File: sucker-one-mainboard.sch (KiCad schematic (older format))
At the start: 114 parts, among them J1 JST NC Valve, J10 JST Motor, J11 User Interface Module, J12 SWD, J2 JST NO Valve, J3 6P4C, J4 JST 3 Way Valve, J5 EXP Port, Q1 BSS138, Q2 BSS138, Q3 BSS138, Q4 DMN15H310SE-13, SW1 Power Switch, SW2 Reset, U1 LD1117S33TR, U2 TPS61087DRCR, U3 STM32F103RBTx, U4 2SMPP-03, U5 INA125UA, Y1 8MHz(16pf)

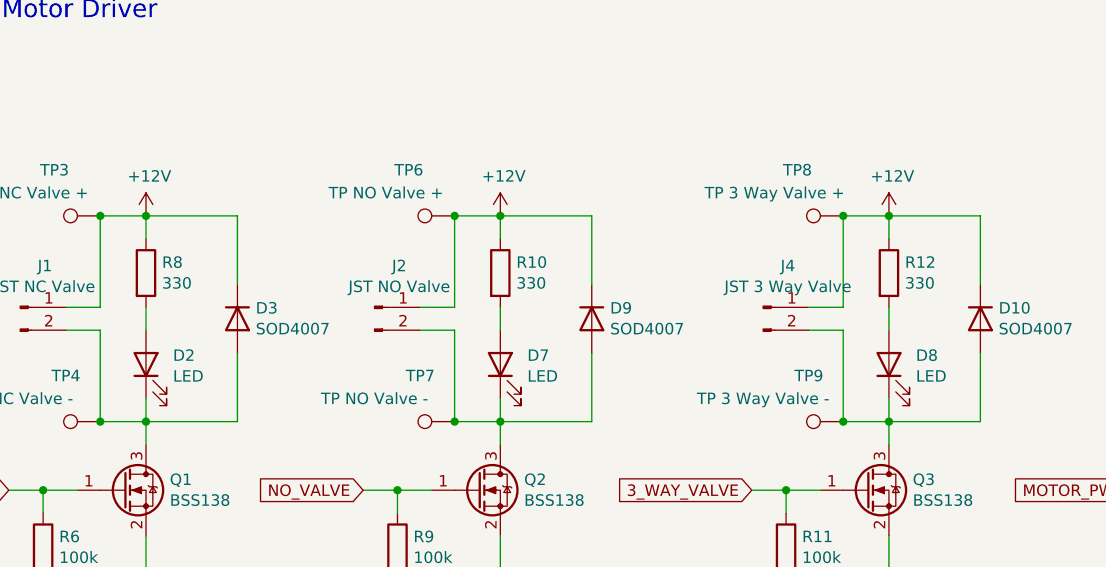
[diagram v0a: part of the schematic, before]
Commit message: Dim LEDs by increasing their resistor values
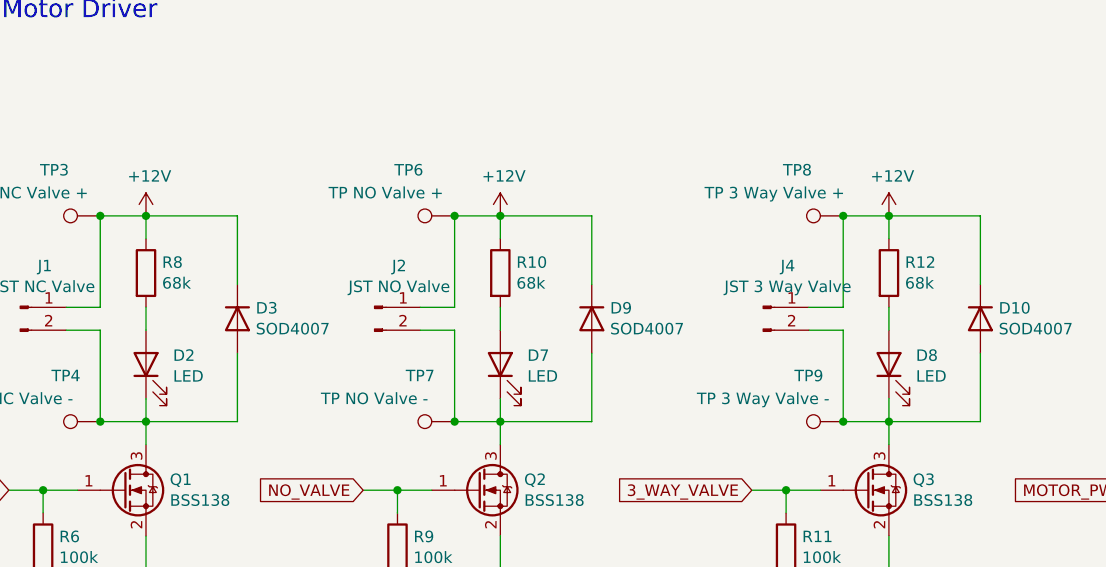
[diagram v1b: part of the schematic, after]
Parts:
- R10, R12, R8: value 330 -> 68k
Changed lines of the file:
@@
 P 4550 1750
 F 0 "R8" H 4620 1796 50  0000 L CNN
-F 1 "330" H 4620 1705 50  0000 L CNN
+F 1 "68k" H 4620 1705 50  0000 L CNN
 F 2 "Resistor_SMD:R_0603_1608Metric_Pad0.98x0.95mm_HandSolder" V 4480 1750 50  0001 C CNN
 F 3 "~" H 4550 1750 50  0001 C CNN
@@
 P 6100 1750
 F 0 "R10" H 6170 1796 50  0000 L CNN
-F 1 "330" H 6170 1705 50  0000 L CNN
+F 1 "68k" H 6170 1705 50  0000 L CNN
 F 2 "Resistor_SMD:R_0603_1608Metric_Pad0.98x0.95mm_HandSolder" V 6030 1750 50  0001 C CNN
 F 3 "~" H 6100 1750 50  0001 C CNN
@@
 P 7800 1750
 F 0 "R12" H 7870 1796 50  0000 L CNN
-F 1 "330" H 7870 1705 50  0000 L CNN
+F 1 "68k" H 7870 1705 50  0000 L CNN
 F 2 "Resistor_SMD:R_0603_1608Metric_Pad0.98x0.95mm_HandSolder" V 7730 1750 50  0001 C CNN
 F 3 "~" H 7800 1750 50  0001 C CNN

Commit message: Fix both fuse footprints (they were swapped)
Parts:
- F1: footprint Fuse:Fuse_1210_3225Metric_Pad1.42x2.65mm_HandSolder -> Fuse:Fuse_1812_4532Metric_Pad1.30x3.40mm_HandSolder
- F2: footprint Fuse:Fuse_1812_4532Metric_Pad1.30x3.40mm_HandSolder -> Fuse:Fuse_1210_3225Metric_Pad1.42x2.65mm_HandSolder
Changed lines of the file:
@@
 F 0 "F2" V 3425 8300 50  0000 C CNN
 F 1 "1210L150THWR" V 3334 8300 50  0000 C CNN
-F 2 "Fuse:Fuse_1812_4532Metric_Pad1.30x3.40mm_HandSolder" H 3250 8100 50  0001 L CNN
+F 2 "Fuse:Fuse_1210_3225Metric_Pad1.42x2.65mm_HandSolder" H 3250 8100 50  0001 L CNN
 F 3 "~" H 3200 8300 50  0001 C CNN
 F 4 "" V 3200 8300 50  0001 C CNN "Field4"
@@
 F 0 "F1" V 3150 6750 50  0000 C CNN
 F 1 "1812L075PR" V 3050 6550 50  0000 C CNN
-F 2 "Fuse:Fuse_1210_3225Metric_Pad1.42x2.65mm_HandSolder" H 3250 6350 50  0001 L CNN
+F 2 "Fuse:Fuse_1812_4532Metric_Pad1.30x3.40mm_HandSolder" H 3250 6350 50  0001 L CNN
 F 3 "~" H 3200 6550 50  0001 C CNN
 F 4 "" V 3200 6550 50  0001 C CNN "Field4"

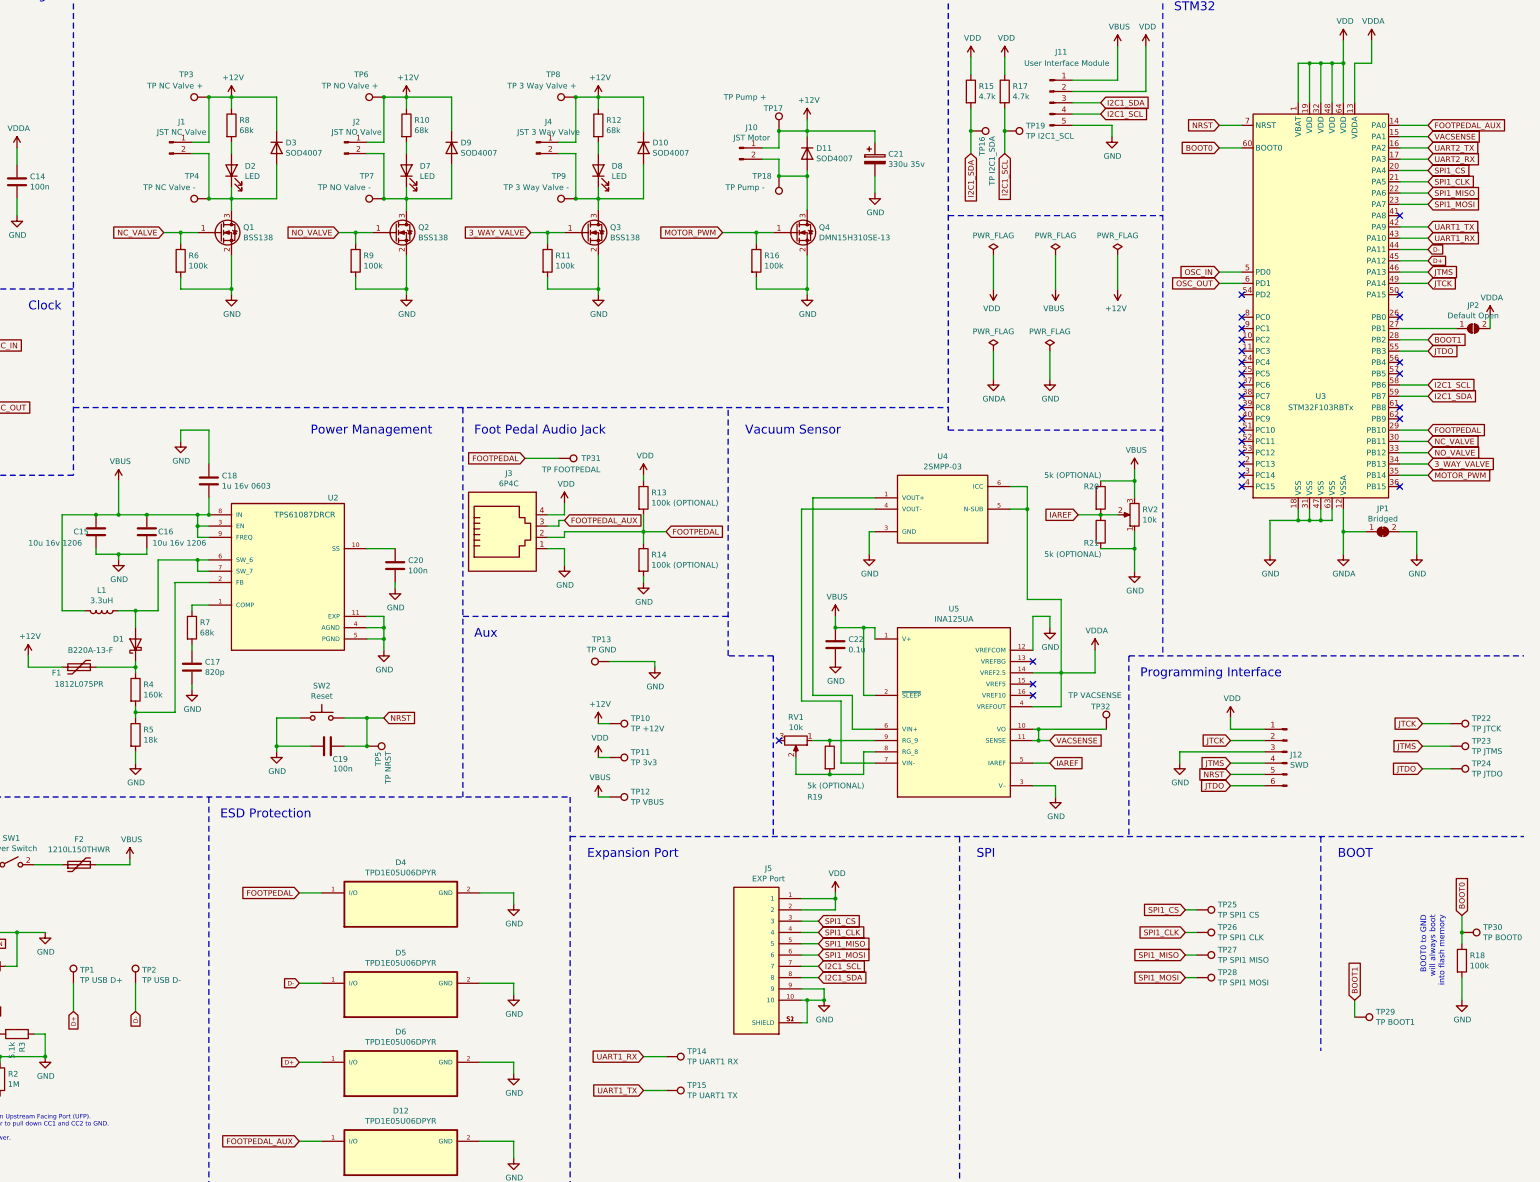
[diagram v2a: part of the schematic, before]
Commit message: Update silkscreen labels
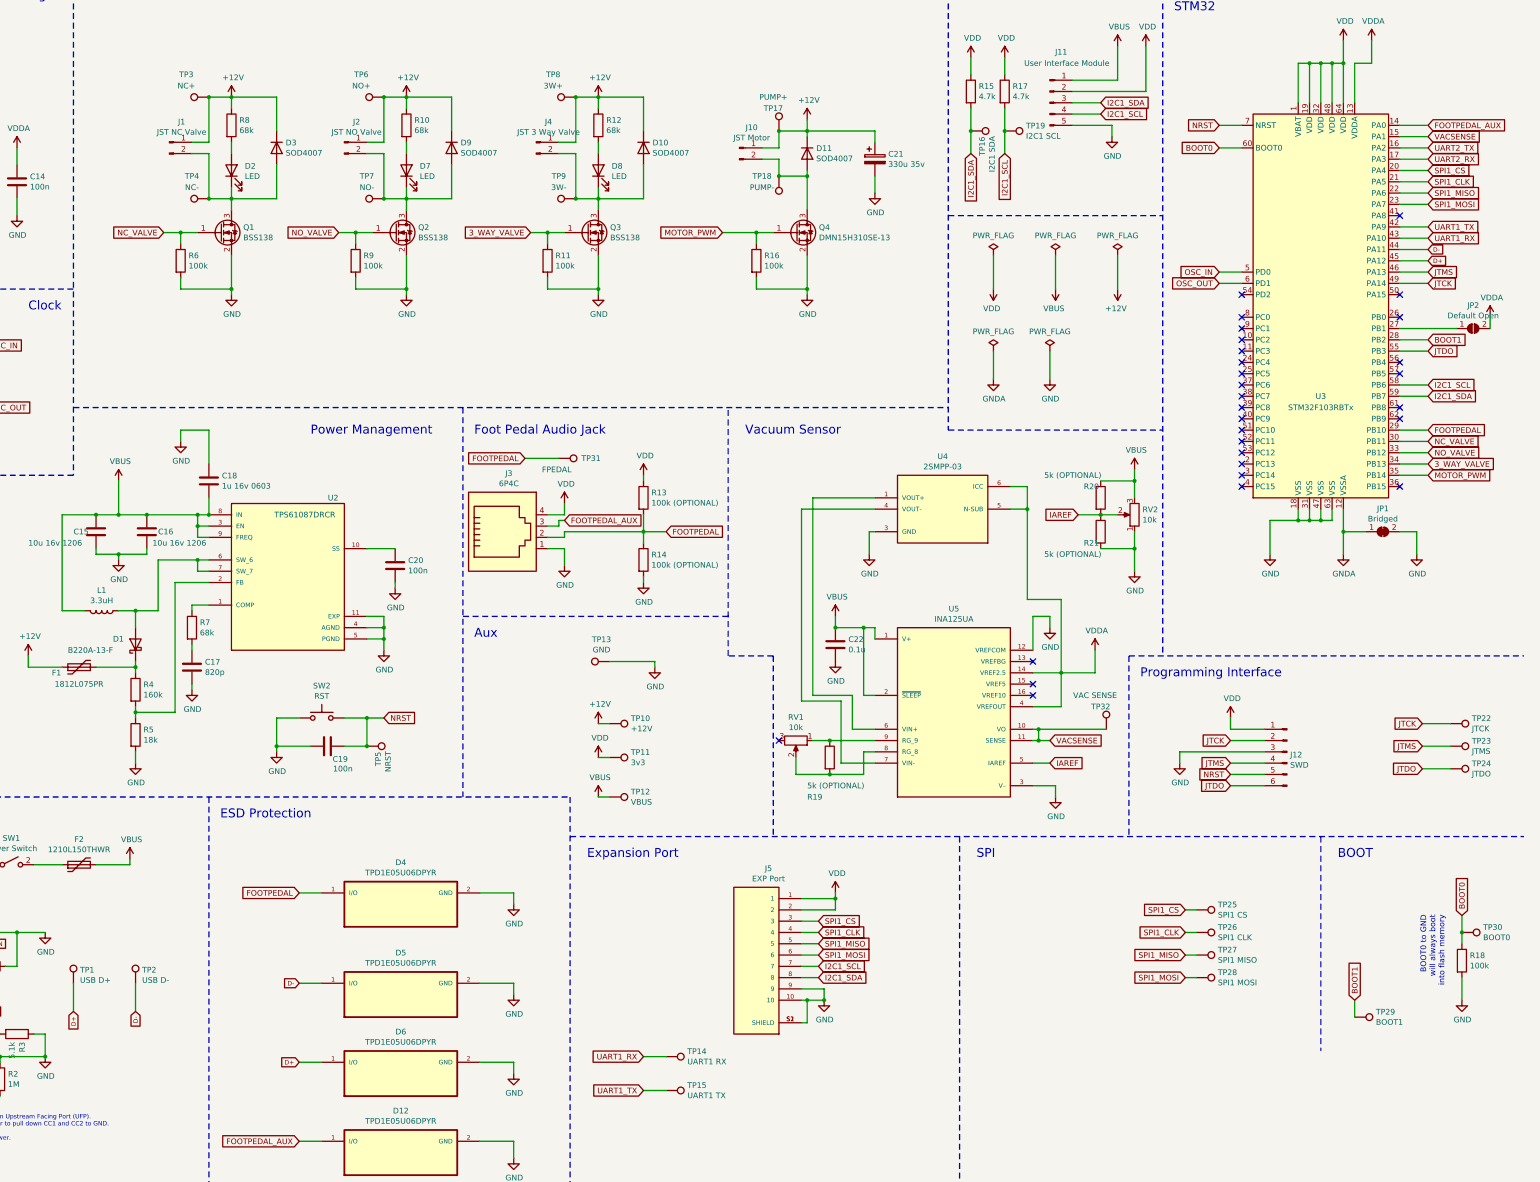
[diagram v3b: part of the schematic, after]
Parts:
- SW2: value Reset -> RST
- TP1: value TP USB D+ -> USB D+
- TP10: value TP +12V -> +12V
- TP11: value TP 3v3 -> 3v3
- TP12: value TP VBUS -> VBUS
- TP13: value TP GND -> GND
- TP14: value TP UART1 RX -> UART1 RX
- TP15: value TP UART1 TX -> UART1 TX
- TP16: value TP I2C1_SDA -> I2C1 SDA
- TP17: value TP Pump + -> PUMP+
- TP18: value TP Pump - -> PUMP-
- TP19: value TP I2C1_SCL -> I2C1 SCL
- TP2: value TP USB D- -> USB D-
- TP22: value TP JTCK -> JTCK
- TP23: value TP JTMS -> JTMS
- TP24: value TP JTDO -> JTDO
- TP25: value TP SPI1 CS -> SPI1 CS
- TP26: value TP SPI1 CLK -> SPI1 CLK
- TP27: value TP SPI1 MISO -> SPI1 MISO
- TP28: value TP SPI1 MOSI -> SPI1 MOSI
- TP29: value TP BOOT1 -> BOOT1
- TP3: value TP NC Valve + -> NC+
- TP30: value TP BOOT0 -> BOOT0
- TP31: value TP FOOTPEDAL -> FPEDAL
- TP32: value TP VACSENSE -> VAC SENSE
- TP4: value TP NC Valve - -> NC-
- TP5: value TP NRST -> NRST
- TP6: value TP NO Valve + -> NO+
- TP7: value TP NO Valve - -> NO-
- TP8: value TP 3 Way Valve + -> 3W+
- TP9: value TP 3 Way Valve - -> 3W-
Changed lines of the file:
@@
 P 5350 7000
 F 0 "SW2" H 5350 7285 50  0000 C CNN
-F 1 "Reset" H 5350 7194 50  0000 C CNN
+F 1 "RST" H 5350 7194 50  0000 C CNN
 F 2 "Button_Switch_SMD:SW_SPST_B3U-1000P" H 5350 7200 50  0001 C CNN
 F 3 "~" H 5350 7200 50  0001 C CNN
@@
 P 7900 7050
 F 0 "TP10" V 7854 7238 50  0000 L CNN
-F 1 "TP +12V" V 7945 7238 50  0000 L CNN
+F 1 "+12V" V 7945 7238 50  0000 L CNN
 F 2 "TestPoint:TestPoint_Pad_D2.0mm" H 8100 7050 50  0001 C CNN
 F 3 "~" H 8100 7050 50  0001 C CNN
@@
 P 7900 7350
 F 0 "TP11" V 7854 7538 50  0000 L CNN
-F 1 "TP 3v3" V 7945 7538 50  0000 L CNN
+F 1 "3v3" V 7945 7538 50  0000 L CNN
 F 2 "TestPoint:TestPoint_Pad_D2.0mm" H 8100 7350 50  0001 C CNN
 F 3 "~" H 8100 7350 50  0001 C CNN
@@
 P 7900 7700
 F 0 "TP12" V 7854 7888 50  0000 L CNN
-F 1 "TP VBUS" V 7945 7888 50  0000 L CNN
+F 1 "VBUS" V 7945 7888 50  0000 L CNN
 F 2 "TestPoint:TestPoint_Pad_D2.0mm" H 8100 7700 50  0001 C CNN
 F 3 "~" H 8100 7700 50  0001 C CNN
@@
 P 11400 1800
 F 0 "TP19" V 11354 1988 50  0000 L CNN
-F 1 "TP I2C1_SCL" V 11445 1988 50  0000 L CNN
+F 1 "I2C1 SCL" V 11445 1988 50  0000 L CNN
 F 2 "TestPoint:TestPoint_Pad_D2.0mm" H 11600 1800 50  0001 C CNN
 F 3 "~" H 11600 1800 50  0001 C CNN
@@
 P 11100 1800
 F 0 "TP16" H 11150 1900 50  0000 L CNN
-F 1 "TP I2C1_SDA" H 11145 1988 50  0000 L CNN
+F 1 " I2C1 SDA" H 11145 1988 50  0000 L CNN
 F 2 "TestPoint:TestPoint_Pad_D2.0mm" H 11300 1800 50  0001 C CNN
 F 3 "~" H 11300 1800 50  0001 C CNN
@@
 P 4350 1500
 F 0 "TP3" V 4550 1700 50  0000 C CNN
-F 1 "TP NC Valve +" V 4450 1800 50  0000 C CNN
+F 1 "NC+" V 4450 1700 50  0000 C CNN
 F 2 "TestPoint:TestPoint_Pad_D2.0mm" H 4550 1500 50  0001 C CNN
 F 3 "~" H 4550 1500 50  0001 C CNN
@@
 P 4350 2400
 F 0 "TP4" V 4550 2550 50  0000 C CNN
-F 1 "TP NC Valve -" V 4450 2750 50  0000 C CNN
+F 1 "NC-" V 4450 2550 50  0000 C CNN
 F 2 "TestPoint:TestPoint_Pad_D2.0mm" H 4550 2400 50  0001 C CNN
 F 3 "~" H 4550 2400 50  0001 C CNN
@@
 P 5900 2400
 F 0 "TP7" V 6100 2550 50  0000 C CNN
-F 1 "TP NO Valve -" V 6000 2750 50  0000 C CNN
+F 1 "NO-" V 6000 2550 50  0000 C CNN
 F 2 "TestPoint:TestPoint_Pad_D2.0mm" H 6100 2400 50  0001 C CNN
 F 3 "~" H 6100 2400 50  0001 C CNN
@@
 P 5900 1500
 F 0 "TP6" V 6100 1700 50  0000 C CNN
-F 1 "TP NO Valve +" V 6000 1800 50  0000 C CNN
+F 1 "NO+" V 6000 1700 50  0000 C CNN
 F 2 "TestPoint:TestPoint_Pad_D2.0mm" H 6100 1500 50  0001 C CNN
 F 3 "~" H 6100 1500 50  0001 C CNN
@@
 P 7600 1500
 F 0 "TP8" V 7800 1700 50  0000 C CNN
-F 1 "TP 3 Way Valve +" V 7700 1800 50  0000 C CNN
+F 1 "3W+" V 7700 1700 50  0000 C CNN
 F 2 "TestPoint:TestPoint_Pad_D2.0mm" H 7800 1500 50  0001 C CNN
 F 3 "~" H 7800 1500 50  0001 C CNN
@@
 P 7600 2400
 F 0 "TP9" V 7800 2550 50  0000 C CNN
-F 1 "TP 3 Way Valve -" V 7700 2750 50  0000 C CNN
+F 1 "3W-" V 7700 2550 50  0000 C CNN
 F 2 "TestPoint:TestPoint_Pad_D2.0mm" H 7800 2400 50  0001 C CNN
 F 3 "~" H 7800 2400 50  0001 C CNN
@@
 P 9400 1800
 F 0 "TP17" H 9350 2000 50  0000 C CNN
-F 1 "TP Pump +" H 9100 2100 50  0000 C CNN
+F 1 "PUMP+" H 9350 2100 50  0000 C CNN
 F 2 "TestPoint:TestPoint_Pad_D2.0mm" H 9600 1800 50  0001 C CNN
 F 3 "~" H 9600 1800 50  0001 C CNN
@@
 P 9400 2200
 F 0 "TP18" H 9550 2200 50  0000 C CNN
-F 1 "TP Pump -" H 9700 2300 50  0000 C CNN
+F 1 "PUMP-" H 9550 2300 50  0000 C CNN
 F 2 "TestPoint:TestPoint_Pad_D2.0mm" H 9600 2200 50  0001 C CNN
 F 3 "~" H 9600 2200 50  0001 C CNN
@@
 P 3150 9350
 F 0 "TP1" H 3208 9468 50  0000 L CNN
-F 1 "TP USB D+" H 3208 9377 50  0000 L CNN
+F 1 "USB D+" H 3208 9377 50  0000 L CNN
 F 2 "TestPoint:TestPoint_Pad_D2.0mm" H 3350 9350 50  0001 C CNN
 F 3 "~" H 3350 9350 50  0001 C CNN
@@
 P 3700 9350
 F 0 "TP2" H 3758 9468 50  0000 L CNN
-F 1 "TP USB D-" H 3758 9377 50  0000 L CNN
+F 1 "USB D-" H 3758 9377 50  0000 L CNN
 F 2 "TestPoint:TestPoint_Pad_D2.0mm" H 3900 9350 50  0001 C CNN
 F 3 "~" H 3900 9350 50  0001 C CNN
@@
 P 15450 8900
 F 0 "TP30" V 15404 9088 50  0000 L CNN
-F 1 "TP BOOT0" V 15495 9088 50  0000 L CNN
+F 1 "BOOT0" V 15495 9088 50  0000 L CNN
 F 2 "TestPoint:TestPoint_Pad_D2.0mm" H 15650 8900 50  0001 C CNN
 F 3 "~" H 15650 8900 50  0001 C CNN
@@
 P 14500 9650
 F 0 "TP29" V 14454 9838 50  0000 L CNN
-F 1 "TP BOOT1" V 14545 9838 50  0000 L CNN
+F 1 "BOOT1" V 14545 9838 50  0000 L CNN
 F 2 "TestPoint:TestPoint_Pad_D2.0mm" H 14700 9650 50  0001 C CNN
 F 3 "~" H 14700 9650 50  0001 C CNN
@@
 P 5750 7250
 F 0 "TP5" H 5800 7350 50  0000 L CNN
-F 1 "TP NRST" H 5795 7438 50  0000 L CNN
+F 1 "NRST" H 5795 7438 50  0000 L CNN
 F 2 "TestPoint:TestPoint_Pad_D2.0mm" H 5950 7250 50  0001 C CNN
 F 3 "~" H 5950 7250 50  0001 C CNN
@@
 P 15350 7050
 F 0 "TP22" V 15304 7238 50  0000 L CNN
-F 1 "TP JTCK" V 15395 7238 50  0000 L CNN
+F 1 "JTCK" V 15395 7238 50  0000 L CNN
 F 2 "TestPoint:TestPoint_Pad_D2.0mm" H 15550 7050 50  0001 C CNN
 F 3 "~" H 15550 7050 50  0001 C CNN
@@
 P 15350 7250
 F 0 "TP23" V 15304 7438 50  0000 L CNN
-F 1 "TP JTMS" V 15395 7438 50  0000 L CNN
+F 1 "JTMS" V 15395 7438 50  0000 L CNN
 F 2 "TestPoint:TestPoint_Pad_D2.0mm" H 15550 7250 50  0001 C CNN
 F 3 "~" H 15550 7250 50  0001 C CNN
@@
 P 15350 7450
 F 0 "TP24" V 15304 7638 50  0000 L CNN
-F 1 "TP JTDO" V 15395 7638 50  0000 L CNN
+F 1 "JTDO" V 15395 7638 50  0000 L CNN
 F 2 "TestPoint:TestPoint_Pad_D2.0mm" H 15550 7450 50  0001 C CNN
 F 3 "~" H 15550 7450 50  0001 C CNN
@@
 P 7900 6500
 F 0 "TP13" V 8095 6572 50  0000 C CNN
-F 1 "TP GND" V 8004 6572 50  0000 C CNN
+F 1 "GND" V 8004 6572 50  0000 C CNN
 F 2 "TestPoint:TestPoint_Pad_D2.0mm" H 8100 6500 50  0001 C CNN
 F 3 "~" H 8100 6500 50  0001 C CNN
@@
 P 8400 10000
 F 0 "TP14" V 8354 10188 50  0000 L CNN
-F 1 "TP UART1 RX" V 8445 10188 50  0000 L CNN
+F 1 "UART1 RX" V 8445 10188 50  0000 L CNN
 F 2 "TestPoint:TestPoint_Pad_D2.0mm" H 8600 10000 50  0001 C CNN
 F 3 "~" H 8600 10000 50  0001 C CNN
@@
 P 8400 10300
 F 0 "TP15" V 8354 10488 50  0000 L CNN
-F 1 "TP UART1 TX" V 8445 10488 50  0000 L CNN
+F 1 "UART1 TX" V 8445 10488 50  0000 L CNN
 F 2 "TestPoint:TestPoint_Pad_D2.0mm" H 8600 10300 50  0001 C CNN
 F 3 "~" H 8600 10300 50  0001 C CNN
@@
 P 13100 8700
 F 0 "TP25" V 13054 8888 50  0000 L CNN
-F 1 "TP SPI1 CS" V 13145 8888 50  0000 L CNN
+F 1 "SPI1 CS" V 13145 8888 50  0000 L CNN
 F 2 "TestPoint:TestPoint_Pad_D2.0mm" H 13300 8700 50  0001 C CNN
 F 3 "~" H 13300 8700 50  0001 C CNN
@@
 P 13100 8900
 F 0 "TP26" V 13054 9088 50  0000 L CNN
-F 1 "TP SPI1 CLK" V 13145 9088 50  0000 L CNN
+F 1 "SPI1 CLK" V 13145 9088 50  0000 L CNN
 F 2 "TestPoint:TestPoint_Pad_D2.0mm" H 13300 8900 50  0001 C CNN
 F 3 "~" H 13300 8900 50  0001 C CNN
@@
 P 13100 9100
 F 0 "TP27" V 13054 9288 50  0000 L CNN
-F 1 "TP SPI1 MISO" V 13145 9288 50  0000 L CNN
+F 1 "SPI1 MISO" V 13145 9288 50  0000 L CNN
 F 2 "TestPoint:TestPoint_Pad_D2.0mm" H 13300 9100 50  0001 C CNN
 F 3 "~" H 13300 9100 50  0001 C CNN
@@
 P 13100 9300
 F 0 "TP28" V 13054 9488 50  0000 L CNN
-F 1 "TP SPI1 MOSI" V 13145 9488 50  0000 L CNN
+F 1 "SPI1 MOSI" V 13145 9488 50  0000 L CNN
 F 2 "TestPoint:TestPoint_Pad_D2.0mm" H 13300 9300 50  0001 C CNN
 F 3 "~" H 13300 9300 50  0001 C CNN
@@
 P 7450 4700
 F 0 "TP31" V 7450 4900 50  0000 L CNN
-F 1 "TP FOOTPEDAL" V 7550 4550 50  0000 L CNN
+F 1 "FPEDAL" V 7550 4550 50  0000 L CNN
 F 2 "TestPoint:TestPoint_Pad_D2.0mm" H 7650 4700 50  0001 C CNN
 F 3 "~" H 7650 4700 50  0001 C CNN
@@
 P 12300 7100
 F 0 "TP32" H 12250 7300 50  0000 C CNN
-F 1 "TP VACSENSE" H 12200 7400 50  0000 C CNN
+F 1 "VAC SENSE" H 12200 7400 50  0000 C CNN
 F 2 "TestPoint:TestPoint_Pad_D2.0mm" H 12500 7100 50  0001 C CNN
 F 3 "~" H 12500 7100 50  0001 C CNN
